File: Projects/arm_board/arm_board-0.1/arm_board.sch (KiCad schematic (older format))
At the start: 9 parts, among them P3 CONN_2, P4 CONN_2, U1 TLV150X, U2 7805, U56 2534-6002UB_34-pin_header

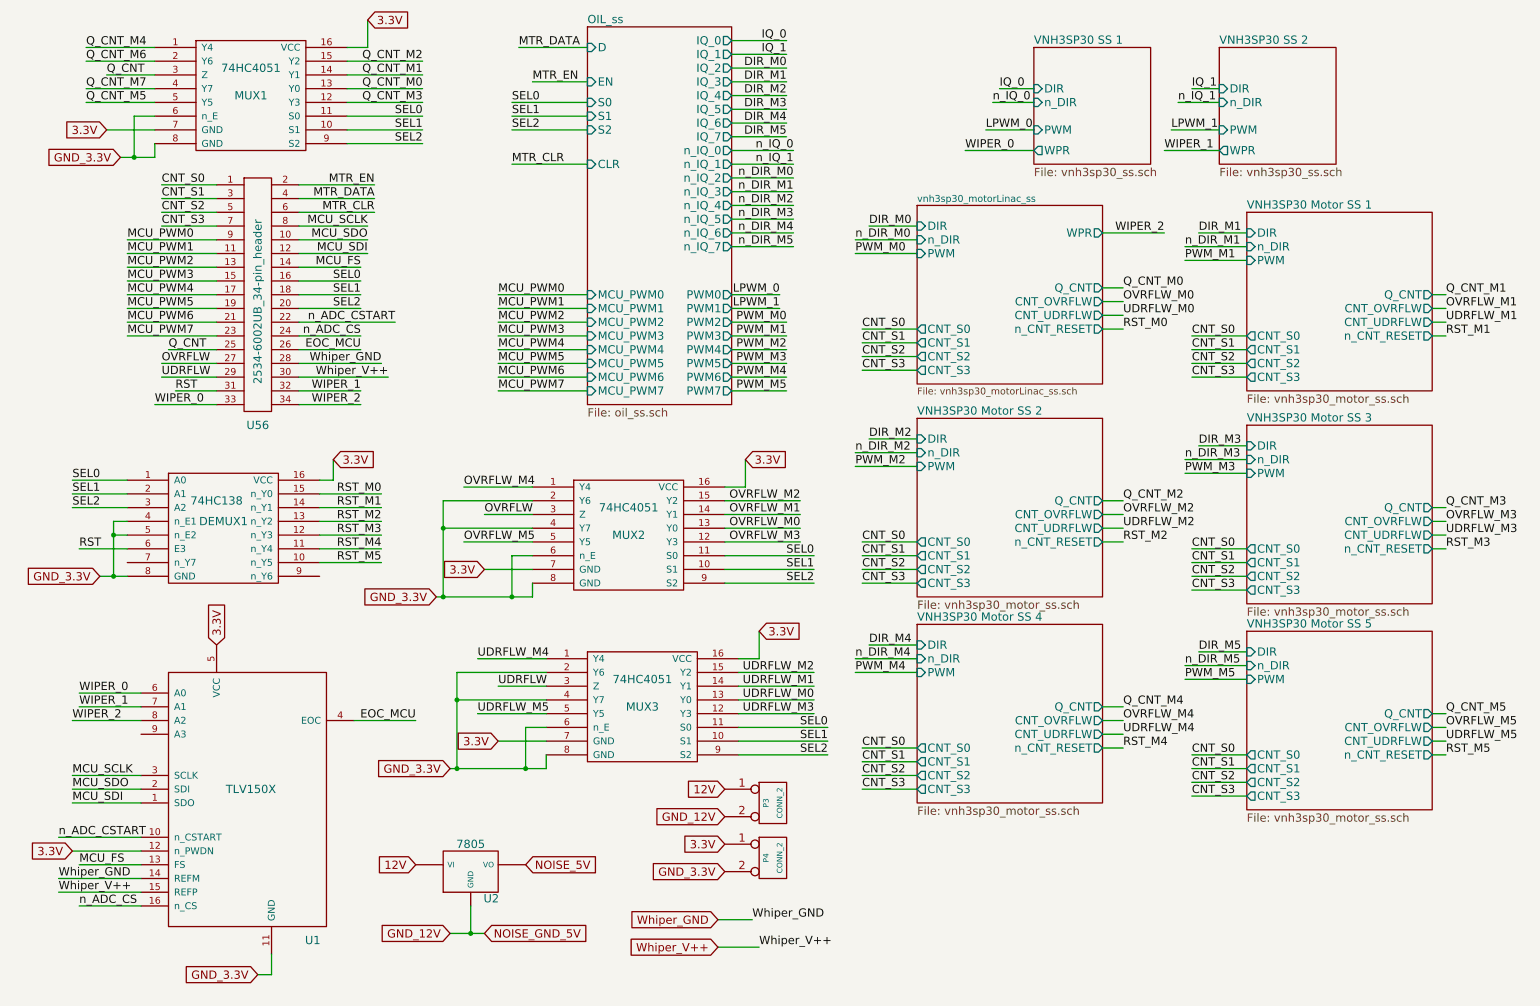
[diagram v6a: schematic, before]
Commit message: Arm Board: finalizing footprints.
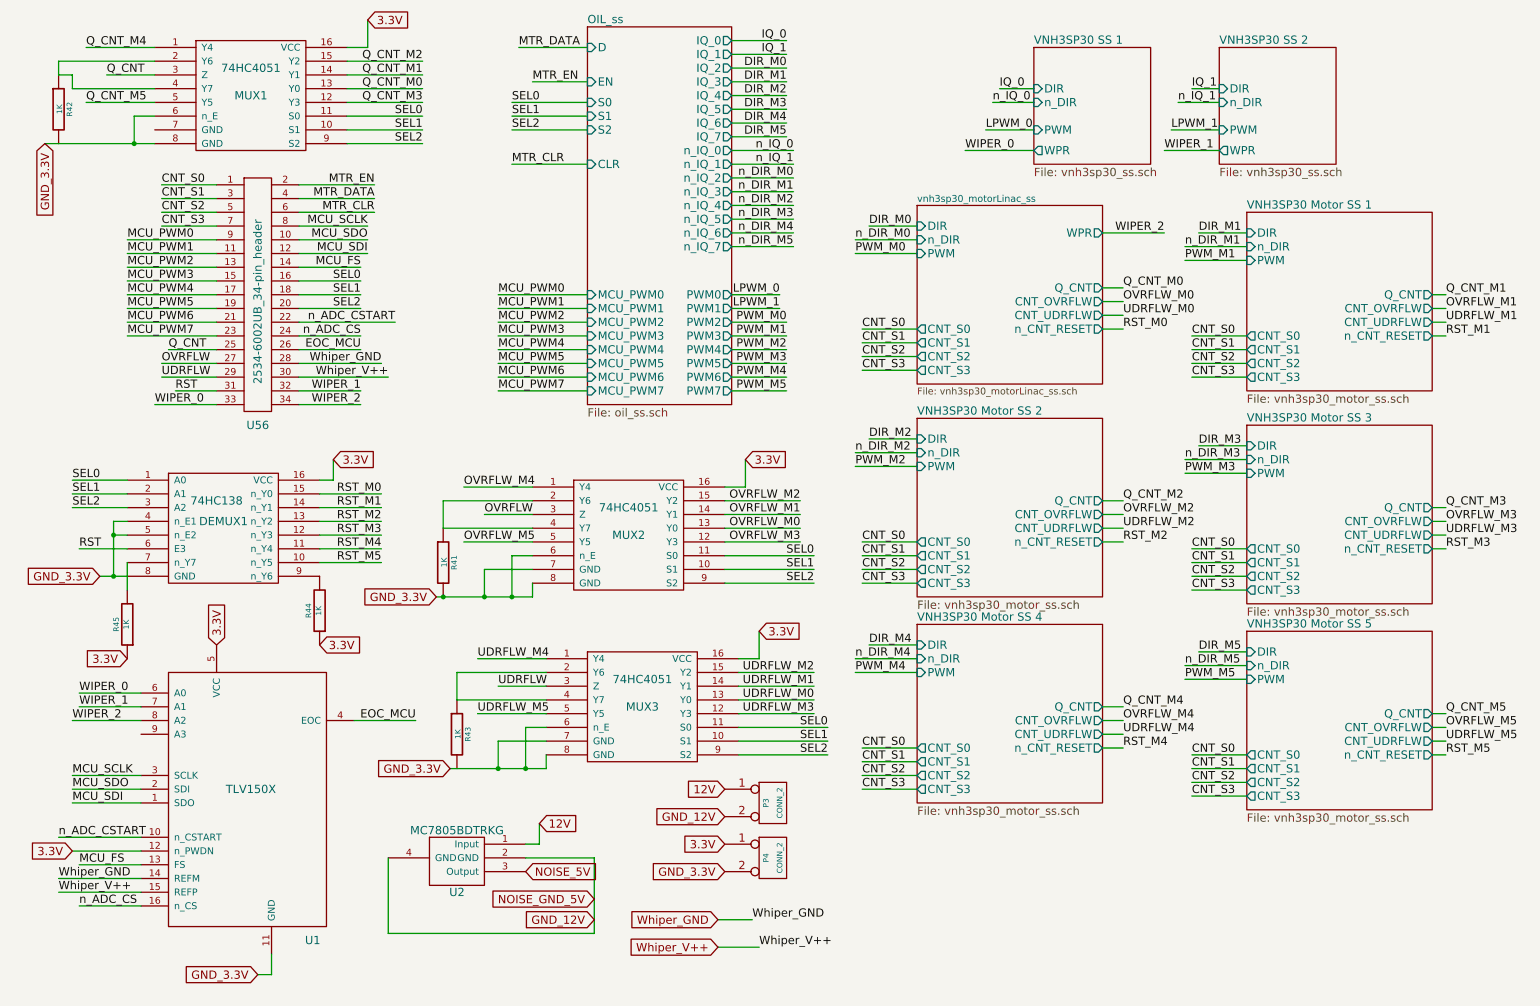
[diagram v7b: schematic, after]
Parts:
- removed U2: 7805, ArmFootprints:MC7805CDTRKG, symbol 7805
- added R41, R42, R43, R44, R45: 1K, Resistors_SMD:R_0805, symbol R
- added U2: MC7805BDTRKG, ArmFootprints:MC7805CDTRKG, symbol MC7805BDTRKG
- DEMUX1, MUX1, MUX2, MUX3, U1: footprint SMD_Packages:SO-16-N -> ArmFootprints:SOIC-16
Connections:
- net Q_CNT_M7 is gone; now on an unnamed net: MUX1.4 (Y7)
- net 12V: now also U2.1 (Input)
- net 3.3V: now also R44.1, R45.1; no longer MUX1.7 (GND), MUX2.7 (GND), MUX3.7 (GND)
- net GND_12V: now also U2.2 (GND), U2.4 (GND)
- net GND_3.3V: now also MUX2.7 (GND), MUX3.7 (GND), R41.2; no longer MUX2.2 (Y6), MUX2.4 (Y7), MUX3.2 (Y6), MUX3.4 (Y7)
- net NOISE_5V: now also U2.3 (Output)
- net at DEMUX1.7 (n_Y7): now also R45.2
- net at DEMUX1.9 (n_Y6): now also R44.2
- net Q_CNT_M6: no longer names the net of MUX1.2 (Y6)
- net Q_CNT_M6: now also R42.1
- new net: MUX2.2 (Y6), MUX2.4 (Y7), R41.1
- new net: MUX3.2 (Y6), MUX3.4 (Y7), R43.1
